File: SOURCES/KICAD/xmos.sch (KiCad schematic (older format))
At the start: 76 parts, among them IC401 IC_NC7WZ07, IC402 NC7SZ175, IC403 IC_XE216-512-TQ128, IC404 IC_CS2100CP, IC405 NC7SZ157, IC406 NC7SZ157, IC407 IC_NCP4681DSQ25T1G, IC408 IC_IS25LP080D, IC409 IC_NCP1117LPST33, IC410 IC_TLV62565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

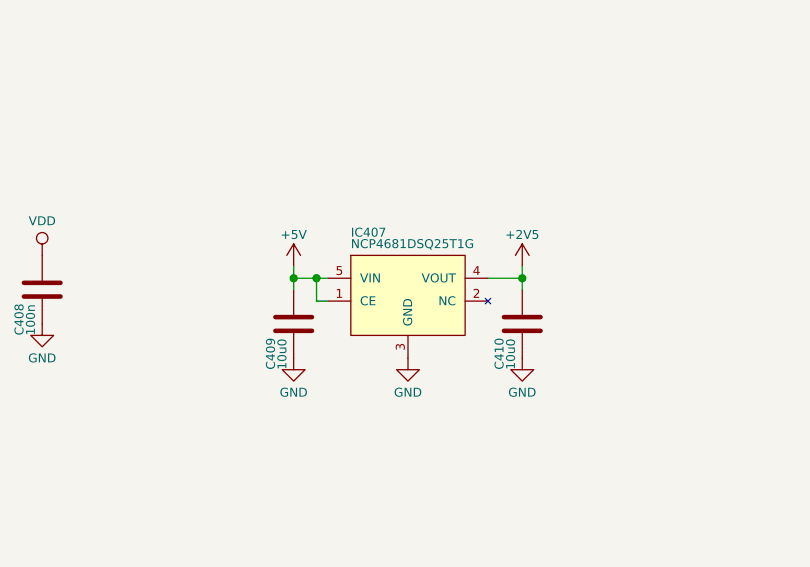
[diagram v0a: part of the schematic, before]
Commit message: Replaced obsolete +2V5 Reg
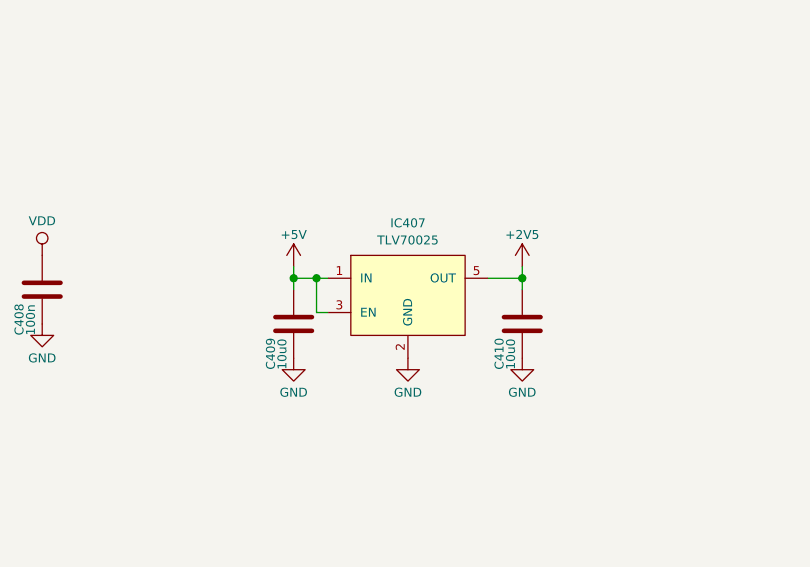
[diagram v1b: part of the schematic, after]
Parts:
- removed IC407: IC_NCP4681DSQ25T1G, TO_SOT_Packages_SMD:SC-70-5, symbol rk:IC_NCP4681DSQ25T1G
- added IC407: TLV70025, rklib:SC70-5, symbol rkdev:TLV70025
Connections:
- net +2V5: now also IC407.5 (OUT)
- net +5V: now also IC407.1 (IN), IC407.3 (EN)
- net GND: now also IC407.2 (GND)
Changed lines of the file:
@@
 Connection ~ 10700 7550
 Wire Wire Line
-	9850 7650 9800 7650
-Wire Wire Line
-	9800 7650 9800 7550
+	9850 7700 9800 7700
+Wire Wire Line
+	9800 7700 9800 7550
 Connection ~ 9800 7550
 Wire Wire Line
@@
 F 8 "IS25LP080D-JNLE" H 0   0   50  0001 C CNN "pn"
 	1    7850 7650
-	1    0    0    -1
-$EndComp
-$Comp
-L rk:IC_NCP4681DSQ25T1G IC407
-U 1 1 5E44788A
-P 10200 7600
-F 0 "IC407" H 9950 7850 39  0000 L CNN
-F 1 "IC_NCP4681DSQ25T1G" H 10200 7150 39  0001 C CNN
-F 2 "TO_SOT_Packages_SMD:SC-70-5" H 10200 7050 39  0001 C CNN
-F 3 "" H 10550 7200 60  0000 C CNN
-F 4 "NCP4681DSQ25T1G" H 9950 7800 39  0000 L CNN "Value1"
-F 5 "2,5V 150mA" H 10200 7100 39  0001 C CNN "Value2"
-F 6 "NCP4681DSQ25T1GOSCT-ND" H 10200 7000 39  0001 C CNN "digikey"
-F 7 "ON Semiconductor" H 0   0   50  0001 C CNN "Manufacturer"
-F 8 "NCP4681DSQ25T1G" H 0   0   50  0001 C CNN "pn"
-	1    10200 7600
 	1    0    0    -1
 $EndComp
@@
 P 4350 6000
 AR Path="/5B77113C/5CB3676C" Ref="#PWR?"  Part="1"
-AR Path="/5B770691/5CB3676C" Ref="#PWR?"  Part="1"
-F 0 "#PWR?" H 4350 5850 50  0001 C CNN
+AR Path="/5B770691/5CB3676C" Ref="#PWR0276"  Part="1"
+F 0 "#PWR0276" H 4350 5850 50  0001 C CNN
 F 1 "VD" H 4350 6150 39  0000 C CNN
 F 2 "" H 4350 6000 50  0001 C CNN
@@
 	1    0    0    -1
 $EndComp
+$Comp
+L rkdev:TLV70025 IC407
+U 1 1 5CA867CD
+P 10200 7650
+F 0 "IC407" H 10200 7991 39  0000 C CNN
+F 1 "TLV70025" H 10200 7916 39  0000 C CNN
+F 2 "rklib:SC70-5" H 10200 7650 60  0001 C CNN
+F 3 "" H 10200 7650 60  0001 C CNN
+	1    10200 7650
+	1    0    0    -1
+$EndComp

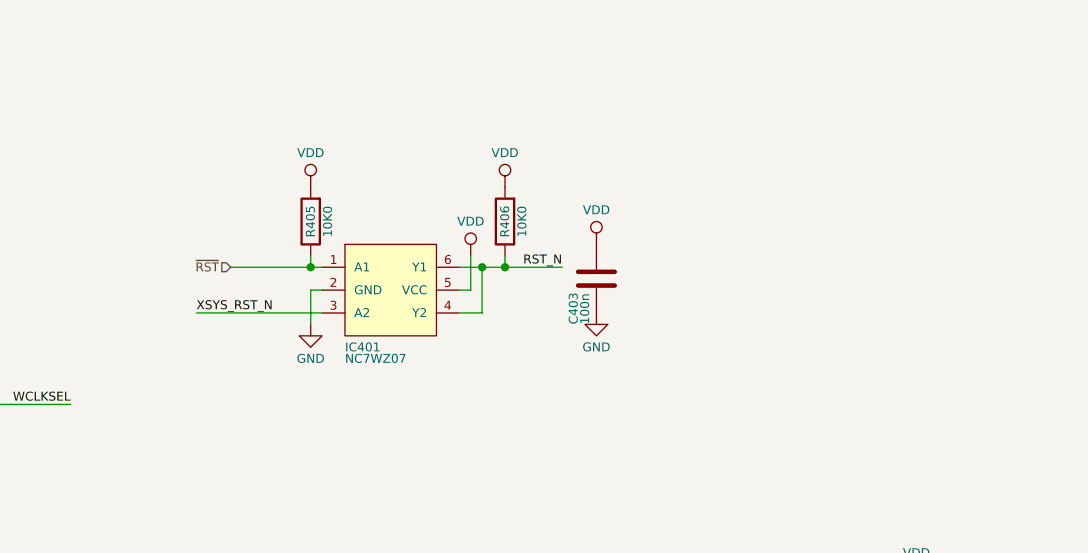
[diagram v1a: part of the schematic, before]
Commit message: Optimized ground plane
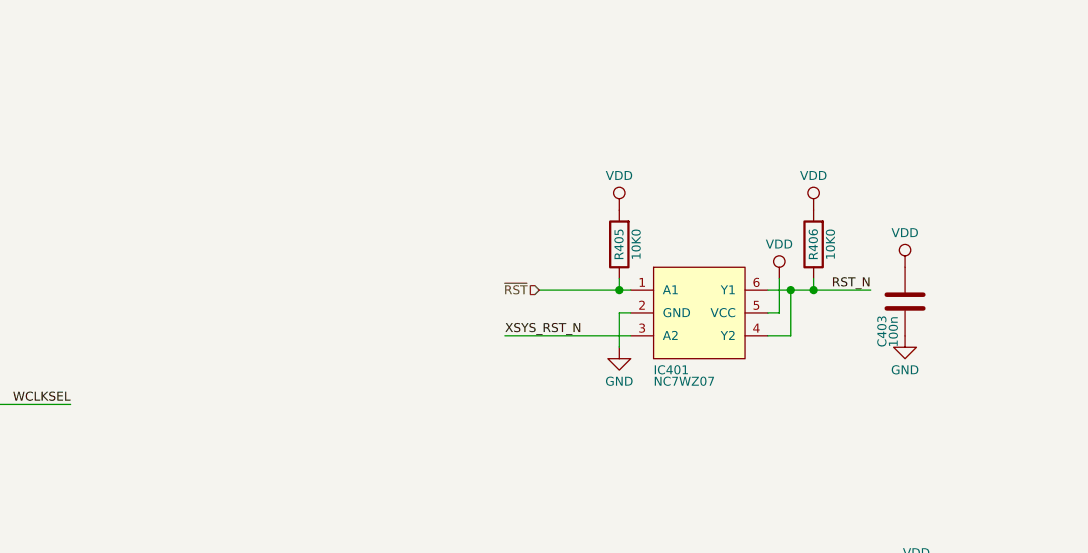
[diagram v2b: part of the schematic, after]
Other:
- moved on the sheet: C403, IC401, R405, R406
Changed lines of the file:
@@
 Text HLabel 4150 6100 3    39   Output ~ 0
 SDA
-Text HLabel 8350 1550 0    39   Input ~ 0
+Text HLabel 9700 1650 0    39   Input ~ 0
 ~RST
 $Comp
@@
 L freeDSP-aurora-rescue:VDD #PWR0253
 U 1 1 5A2CBD87
-P 9400 1500
-F 0 "#PWR0253" H 9400 1350 50  0001 C CNN
-F 1 "VDD" H 9400 1650 39  0000 C CNN
-F 2 "" H 9400 1500 50  0000 C CNN
-F 3 "" H 9400 1500 50  0000 C CNN
-	1    9400 1500
+P 10750 1600
+F 0 "#PWR0253" H 10750 1450 50  0001 C CNN
+F 1 "VDD" H 10750 1750 39  0000 C CNN
+F 2 "" H 10750 1600 50  0000 C CNN
+F 3 "" H 10750 1600 50  0000 C CNN
+	1    10750 1600
 	1    0    0    -1
 $EndComp
@@
 L freeDSP-aurora-rescue:GND #PWR0254
 U 1 1 5A2CBF11
-P 8700 1800
-F 0 "#PWR0254" H 8700 1550 50  0001 C CNN
-F 1 "GND" H 8700 1650 39  0000 C CNN
-F 2 "" H 8700 1800 50  0000 C CNN
-F 3 "" H 8700 1800 50  0000 C CNN
-	1    8700 1800
+P 10050 1900
+F 0 "#PWR0254" H 10050 1650 50  0001 C CNN
+F 1 "GND" H 10050 1750 39  0000 C CNN
+F 2 "" H 10050 1900 50  0000 C CNN
+F 3 "" H 10050 1900 50  0000 C CNN
+	1    10050 1900
 	1    0    0    -1
 $EndComp
@@
 L freeDSP-aurora-rescue:GND #PWR0255
 U 1 1 5A2CC5EF
-P 9950 1750
-F 0 "#PWR0255" H 9950 1500 50  0001 C CNN
-F 1 "GND" H 9950 1600 39  0000 C CNN
-F 2 "" H 9950 1750 50  0000 C CNN
-F 3 "" H 9950 1750 50  0000 C CNN
-	1    9950 1750
+P 11300 1850
+F 0 "#PWR0255" H 11300 1600 50  0001 C CNN
+F 1 "GND" H 11300 1700 39  0000 C CNN
+F 2 "" H 11300 1850 50  0000 C CNN
+F 3 "" H 11300 1850 50  0000 C CNN
+	1    11300 1850
 	1    0    0    -1
 $EndComp
@@
 L freeDSP-aurora-rescue:VDD #PWR0256
 U 1 1 5A2CC666
-P 9950 1450
-F 0 "#PWR0256" H 9950 1300 50  0001 C CNN
-F 1 "VDD" H 9950 1600 39  0000 C CNN
-F 2 "" H 9950 1450 50  0000 C CNN
-F 3 "" H 9950 1450 50  0000 C CNN
-	1    9950 1450
-	1    0    0    -1
-$EndComp
-Text Label 8200 1750 0    39   ~ 0
+P 11300 1550
+F 0 "#PWR0256" H 11300 1400 50  0001 C CNN
+F 1 "VDD" H 11300 1700 39  0000 C CNN
+F 2 "" H 11300 1550 50  0000 C CNN
+F 3 "" H 11300 1550 50  0000 C CNN
+	1    11300 1550
+	1    0    0    -1
+$EndComp
+Text Label 9550 1850 0    39   ~ 0
 XSYS_RST_N
-Text Label 9800 1550 2    39   ~ 0
+Text Label 11150 1650 2    39   ~ 0
 RST_N
 Text Label 4100 1100 3    39   ~ 0
@@
 L freeDSP-aurora-rescue:VDD #PWR0257
 U 1 1 5A2CE2EF
-P 8700 1200
-F 0 "#PWR0257" H 8700 1050 50  0001 C CNN
-F 1 "VDD" H 8700 1350 39  0000 C CNN
-F 2 "" H 8700 1200 50  0000 C CNN
-F 3 "" H 8700 1200 50  0000 C CNN
-	1    8700 1200
+P 10050 1300
+F 0 "#PWR0257" H 10050 1150 50  0001 C CNN
+F 1 "VDD" H 10050 1450 39  0000 C CNN
+F 2 "" H 10050 1300 50  0000 C CNN
+F 3 "" H 10050 1300 50  0000 C CNN
+	1    10050 1300
 	1    0    0    -1
 $EndComp
@@
 L freeDSP-aurora-rescue:VDD #PWR0258
 U 1 1 5A2CE32E
-P 9550 1200
-F 0 "#PWR0258" H 9550 1050 50  0001 C CNN
-F 1 "VDD" H 9550 1350 39  0000 C CNN
-F 2 "" H 9550 1200 50  0000 C CNN
-F 3 "" H 9550 1200 50  0000 C CNN
-	1    9550 1200
+P 10900 1300
+F 0 "#PWR0258" H 10900 1150 50  0001 C CNN
+F 1 "VDD" H 10900 1450 39  0000 C CNN
+F 2 "" H 10900 1300 50  0000 C CNN
+F 3 "" H 10900 1300 50  0000 C CNN
+	1    10900 1300
 	1    0    0    -1
 $EndComp
@@
 L freeDSP-aurora-rescue:CAP_100n_50V_X7R_0805 C403
 U 1 1 5AD97284
-P 9950 1600
-F 0 "C403" H 9750 1700 39  0000 L CNN
-F 1 "CAP_100n_50V_X7R_0805" H 9950 1450 39  0001 C CNN
-F 2 "rklib:C0805-X7R" H 9950 1400 39  0001 C CNN
-F 3 "" H 10000 1650 50  0001 C CNN
-F 4 "100n" H 9750 1650 39  0000 L CNN "Value1"
-F 5 "5% 50V X7R" H 9950 1350 39  0001 C CNN "Value2"
-F 6 "399-1170-1-ND" H 9950 1300 39  0001 C CNN "digikey"
-F 7 "KEMET" H 0   0   50  0001 C CNN "Manufacturer"
-F 8 "C0805C104K5RACTU" H 0   0   50  0001 C CNN "pn"
-	1    9950 1600
+P 11300 1700
+F 0 "C403" H 11100 1800 39  0000 L CNN
+F 1 "CAP_100n_50V_X7R_0805" H 11300 1550 39  0001 C CNN
+F 2 "rklib:C0805-X7R" H 11300 1500 39  0001 C CNN
+F 3 "" H 11350 1750 50  0001 C CNN
+F 4 "100n" H 11100 1750 39  0000 L CNN "Value1"
+F 5 "5% 50V X7R" H 11300 1450 39  0001 C CNN "Value2"
+F 6 "399-1170-1-ND" H 11300 1400 39  0001 C CNN "digikey"
+F 7 "KEMET" H 1350 100 50  0001 C CNN "Manufacturer"
+F 8 "C0805C104K5RACTU" H 1350 100 50  0001 C CNN "pn"
+	1    11300 1700
 	0    -1   -1   0
 $EndComp
@@
 L freeDSP-aurora-rescue:RES_10K0_1%_0.25W_Thin_0805 R405
 U 1 1 5AD9DF94
-P 8700 1350
-F 0 "R405" H 8700 1350 39  0000 C CNN
-F 1 "RES_10K0_1%_0.125W_Thick_0805" H 8700 1175 39  0001 C CNN
-F 2 "rklib:C0805-RES" H 8700 1125 39  0001 C CNN
-F 3 "" H 8700 1350 50  0000 C CNN
-F 4 "10K0" H 8700 1275 39  0000 C CNN "Value1"
-F 5 "1% 0.125W Thick" H 8700 1225 39  0001 C CNN "Value2"
-F 6 "311-10.0KCRCT-ND" H 8700 1050 39  0001 C CNN "digikey"
-F 7 "Yageo" H 0   0   50  0001 C CNN "Manufacturer"
-F 8 "RC0805FR-0710KL" H 0   0   50  0001 C CNN "pn"
-	1    8700 1350
+P 10050 1450
+F 0 "R405" H 10050 1450 39  0000 C CNN
+F 1 "RES_10K0_1%_0.125W_Thick_0805" H 10050 1275 39  0001 C CNN
+F 2 "rklib:C0805-RES" H 10050 1225 39  0001 C CNN
+F 3 "" H 10050 1450 50  0000 C CNN
+F 4 "10K0" H 10050 1375 39  0000 C CNN "Value1"
+F 5 "1% 0.125W Thick" H 10050 1325 39  0001 C CNN "Value2"
+F 6 "311-10.0KCRCT-ND" H 10050 1150 39  0001 C CNN "digikey"
+F 7 "Yageo" H 1350 100 50  0001 C CNN "Manufacturer"
+F 8 "RC0805FR-0710KL" H 1350 100 50  0001 C CNN "pn"
+	1    10050 1450
 	0    -1   -1   0
 $EndComp
@@
 L freeDSP-aurora-rescue:RES_10K0_1%_0.25W_Thin_0805 R406
 U 1 1 5AD9E1C1
-P 9550 1350
-F 0 "R406" H 9550 1350 39  0000 C CNN
-F 1 "RES_10K0_1%_0.125W_Thick_0805" H 9550 1175 39  0001 C CNN
-F 2 "rklib:C0805-RES" H 9550 1125 39  0001 C CNN
-F 3 "" H 9550 1350 50  0000 C CNN
-F 4 "10K0" H 9550 1275 39  0000 C CNN "Value1"
-F 5 "1% 0.125W Thick" H 9550 1225 39  0001 C CNN "Value2"
-F 6 "311-10.0KCRCT-ND" H 9550 1050 39  0001 C CNN "digikey"
-F 7 "Yageo" H 0   0   50  0001 C CNN "Manufacturer"
-F 8 "RC0805FR-0710KL" H 0   0   50  0001 C CNN "pn"
-	1    9550 1350
+P 10900 1450
+F 0 "R406" H 10900 1450 39  0000 C CNN
+F 1 "RES_10K0_1%_0.125W_Thick_0805" H 10900 1275 39  0001 C CNN
+F 2 "rklib:C0805-RES" H 10900 1225 39  0001 C CNN
+F 3 "" H 10900 1450 50  0000 C CNN
+F 4 "10K0" H 10900 1375 39  0000 C CNN "Value1"
+F 5 "1% 0.125W Thick" H 10900 1325 39  0001 C CNN "Value2"
+F 6 "311-10.0KCRCT-ND" H 10900 1150 39  0001 C CNN "digikey"
+F 7 "Yageo" H 1350 100 50  0001 C CNN "Manufacturer"
+F 8 "RC0805FR-0710KL" H 1350 100 50  0001 C CNN "pn"
+	1    10900 1450
 	0    -1   -1   0
 $EndComp
@@
 	4150 1500 4150 1700
 Wire Wire Line
-	8350 1550 8700 1550
+	9700 1650 10050 1650
 Connection ~ 4100 1500
 Wire Wire Line
@@
 	5050 8250 5350 8250
 Wire Wire Line
-	9350 1650 9400 1650
-Wire Wire Line
-	9400 1650 9400 1500
-Wire Wire Line
-	8700 1800 8700 1650
-Wire Wire Line
-	8700 1650 8750 1650
-Wire Wire Line
-	8200 1750 8750 1750
-Wire Wire Line
-	9350 1550 9450 1550
-Wire Wire Line
-	9450 1550 9450 1750
-Wire Wire Line
-	9450 1750 9350 1750
-Connection ~ 9450 1550
+	10700 1750 10750 1750
+Wire Wire Line
+	10750 1750 10750 1600
+Wire Wire Line
+	10050 1900 10050 1750
+Wire Wire Line
+	10050 1750 10100 1750
+Wire Wire Line
+	9550 1850 10100 1850
+Wire Wire Line
+	10700 1650 10800 1650
+Wire Wire Line
+	10800 1650 10800 1850
+Wire Wire Line
+	10800 1850 10700 1850
+Connection ~ 10800 1650
 Wire Wire Line
 	4100 1500 4100 1100
 Wire Wire Line
-	9550 1500 9550 1550
-Connection ~ 9550 1550
-Wire Wire Line
-	8700 1500 8700 1550
-Connection ~ 8700 1550
+	10900 1600 10900 1650
+Connection ~ 10900 1650
+Wire Wire Line
+	10050 1600 10050 1650
+Connection ~ 10050 1650
 Wire Wire Line
 	10750 3050 10800 3050
@@
 	9800 7550 9850 7550
 Wire Wire Line
-	9450 1550 9550 1550
-Wire Wire Line
-	9550 1550 9800 1550
-Wire Wire Line
-	8700 1550 8750 1550
+	10800 1650 10900 1650
+Wire Wire Line
+	10900 1650 11150 1650
+Wire Wire Line
+	10050 1650 10100 1650
 Wire Wire Line
 	10800 3050 10800 3150
@@
 L rk:IC_NC7WZ07 IC401
 U 1 1 5C0753FD
-P 9050 1650
-F 0 "IC401" H 8850 1400 39  0000 L CNN
-F 1 "IC_NC7WZ07" H 9050 1250 39  0001 C CNN
-F 2 "TO_SOT_Packages_SMD:SC-70-6" H 9050 1200 39  0001 C CNN
-F 3 "" H 9050 1650 60  0000 C CNN
-F 4 "NC7WZ07" H 8850 1350 39  0000 L CNN "Value1"
-F 5 "Noninverting Buffer" H 9000 1150 39  0001 C CNN "Value2"
-F 6 "NC7WZ07P6XCT-ND" H 9050 1100 39  0001 C CNN "digikey"
-F 7 "ON Semiconductor" H 0   0   50  0001 C CNN "Manufacturer"
-F 8 "NC7WZ07P6X" H 0   0   50  0001 C CNN "pn"
-	1    9050 1650
-	1    0    0    -1
-$EndComp
+P 10400 1750
+F 0 "IC401" H 10200 1500 39  0000 L CNN
+F 1 "IC_NC7WZ07" H 10400 1350 39  0001 C CNN
+F 2 "TO_SOT_Packages_SMD:SC-70-6" H 10400 1300 39  0001 C CNN
+F 3 "" H 10400 1750 60  0000 C CNN
+F 4 "NC7WZ07" H 10200 1450 39  0000 L CNN "Value1"
+F 5 "Noninverting Buffer" H 10350 1250 39  0001 C CNN "Value2"
+F 6 "NC7WZ07P6XCT-ND" H 10400 1200 39  0001 C CNN "digikey"
+F 7 "ON Semiconductor" H 1350 100 50  0001 C CNN "Manufacturer"
+F 8 "NC7WZ07P6X" H 1350 100 50  0001 C CNN "pn"
+	1    10400 1750
+	1    0    0    -1
+$EndComp

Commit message: Updated BOM
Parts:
- IC402: digikey ??? -> 296-16998-1-ND
- IC407: Manufacturer (none) -> Texas Instruments; Value1 (none) -> TLV70025; Value2 (none) -> 2.5V, 200mA; digikey (none) -> 296-27793-1-ND; pn (none) -> TLV70025DCKR
- R407: digikey ??? -> TC164J-33CT-ND
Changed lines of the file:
@@
 F 4 "NC7SZ175" H 0   0   50  0001 C CNN "Value1"
 F 5 "D-Type Flip-Flop with Asynchronous Clear" H 0   0   50  0001 C CNN "Value2"
-F 6 "???" H 0   0   50  0001 C CNN "digikey"
+F 6 "296-16998-1-ND" H 0   0   50  0001 C CNN "digikey"
 F 7 "Texas Instruments" H 0   0   50  0001 C CNN "Manufacturer"
 F 8 "SN74LVC1G175DCKR" H 0   0   50  0001 C CNN "pn"
@@
 F 4 "33R0" V 3100 2350 39  0000 L CNN "Value1"
 F 5 "5% 62,5mW" H 2850 2050 39  0001 C CNN "Value2"
-F 6 "???" H 2850 1950 39  0001 C CNN "digikey"
+F 6 "TC164J-33CT-ND" H 2850 1950 39  0001 C CNN "digikey"
 F 7 "Yageo" H 0   0   50  0001 C CNN "Manufacturer"
 F 8 "TC164-JR-0733RL" H 0   0   50  0001 C CNN "pn"
@@
 F 2 "rklib:SC70-5" H 10200 7650 60  0001 C CNN
 F 3 "" H 10200 7650 60  0001 C CNN
+F 4 "Texas Instruments" H 0   0   50  0001 C CNN "Manufacturer"
+F 5 "296-27793-1-ND" H 0   0   50  0001 C CNN "digikey"
+F 6 "TLV70025DCKR" H 0   0   50  0001 C CNN "pn"
+F 7 "TLV70025" H 0   0   50  0001 C CNN "Value1"
+F 8 "2.5V, 200mA" H 0   0   50  0001 C CNN "Value2"
 	1    10200 7650
 	1    0    0    -1
